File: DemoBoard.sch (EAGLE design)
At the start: 126 parts, among them IC1 LM20125MHE_NOPB, IC2 LM20125MHE_NOPB, J5 DM3AT-SF-PEJM5, J6 SAMTEC-MMS-105-02-X-SVJ, Q1 IRLML0030TRPBF, Q2 MMBT3904,215, Q3 MMBT3904,215, Q4 BC846B,235, Q5 BC846B,235, Q6 BC846B,235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

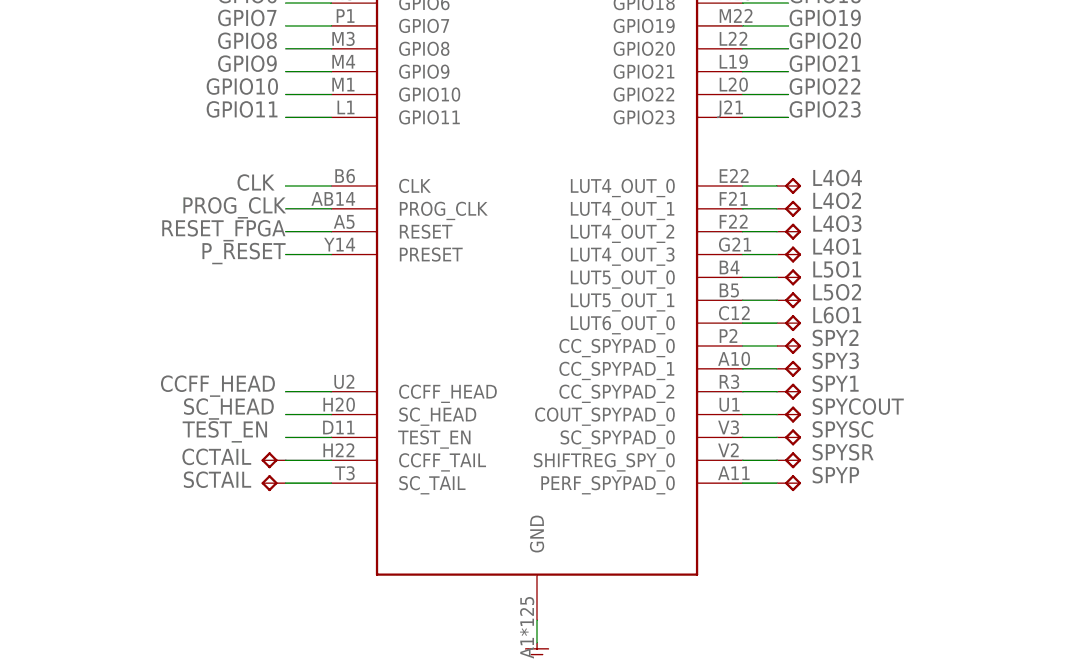
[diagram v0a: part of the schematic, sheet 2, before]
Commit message: Finalize routing, DRC Clean
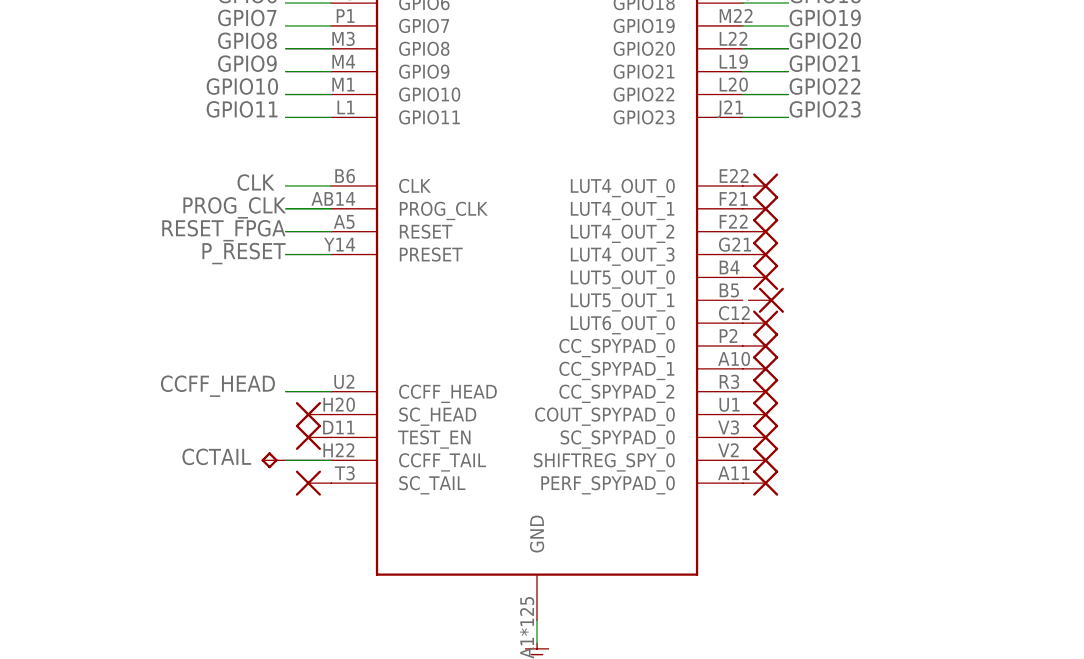
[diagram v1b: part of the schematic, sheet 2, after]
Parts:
- removed L4O1, L4O2, L4O3, L4O4, L5O1, L5O2, L6O1, SCTAIL, SPY1, SPY2, SPY3, SPYCOUT, SPYP, SPYSC, SPYSR: TPPAD1-13, testpad:TPPAD1-13
- added U$74, U$75, U$77, U$78, U$81, U$82, U$85, U$86, U$87, U$88, U$89, U$90, U$91, U$92, U$94, U$95, U$96, U$97, U$98, U$99: NC_MARKER, NC_MARKER:NC_MARKER
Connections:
- removed net SC_HEAD: U3.IO16, U4.SC_HEAD
- removed net TEST_EN: U3.IO26/DAC2/A2_9, U4.TEST_EN
- new net N$72: U$78.P$1, USB1.ID
- new net N$73: U$81.P$1, U3.IO16
- new net N$74: U$82.P$1, U4.TEST_EN
- new net N$75: U$85.P$1, U3.IO17
- net GPIO18: now also J4.3
- net GPIO19: no longer J4.3
- net GPIO21: now also J6.1; no longer J6.2
- net GPIO22: now also J6.2; no longer J6.1
- net GPIO6: now also U3.IO33/A1_5/X32N; no longer U3.IO32/A1_4/X32P
- net GPIO7: now also U3.IO26/DAC2/A2_9; no longer U3.IO17
- net GPIO8: now also U3.IO25/DAC1/A2_8; no longer U3.IO33/A1_5/X32N
- net GPIO9: now also U3.IO32/A1_4/X32P; no longer U3.IO25/DAC1/A2_8
- net N$10: now also U$91.P$1, U4.LUT6_OUT_0; no longer L5O2.TP, U4.LUT5_OUT_1
- net N$11: now also U$92.P$1, U4.CC_SPYPAD_0; no longer L6O1.TP, U4.LUT6_OUT_0
- net N$15: now also U$94.P$1, U4.CC_SPYPAD_1; no longer SPY2.TP, U4.CC_SPYPAD_0
- net N$16: now also U$95.P$1, U4.CC_SPYPAD_2; no longer SPY3.TP, U4.CC_SPYPAD_1
- net N$18: now also U$96.P$1, U4.COUT_SPYPAD_0; no longer SPY1.TP, U4.CC_SPYPAD_2
- net N$19: now also U$97.P$1, U4.SC_SPYPAD_0; no longer SPYCOUT.TP, U4.COUT_SPYPAD_0
- net N$21: now also U$74.P$1, U4.SC_HEAD; no longer SPYSC.TP, U4.SC_SPYPAD_0
- net N$23: now also U$98.P$1; no longer SPYSR.TP
- net N$24: now also U$99.P$1; no longer SPYP.TP
- net N$4: now also U$77.P$1; no longer L4O4.TP
- net N$5: now also U$86.P$1; no longer L4O2.TP
- net N$6: now also U$87.P$1; no longer L4O3.TP
- net N$61: now also U$75.P$1; no longer SCTAIL.TP
- net N$8: now also U$88.P$1; no longer L4O1.TP
- net N$9: now also U$89.P$1; no longer L5O1.TP
